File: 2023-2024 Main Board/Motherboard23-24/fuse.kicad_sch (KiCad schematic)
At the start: 20 parts, among them J22 Conn_01x02_Male

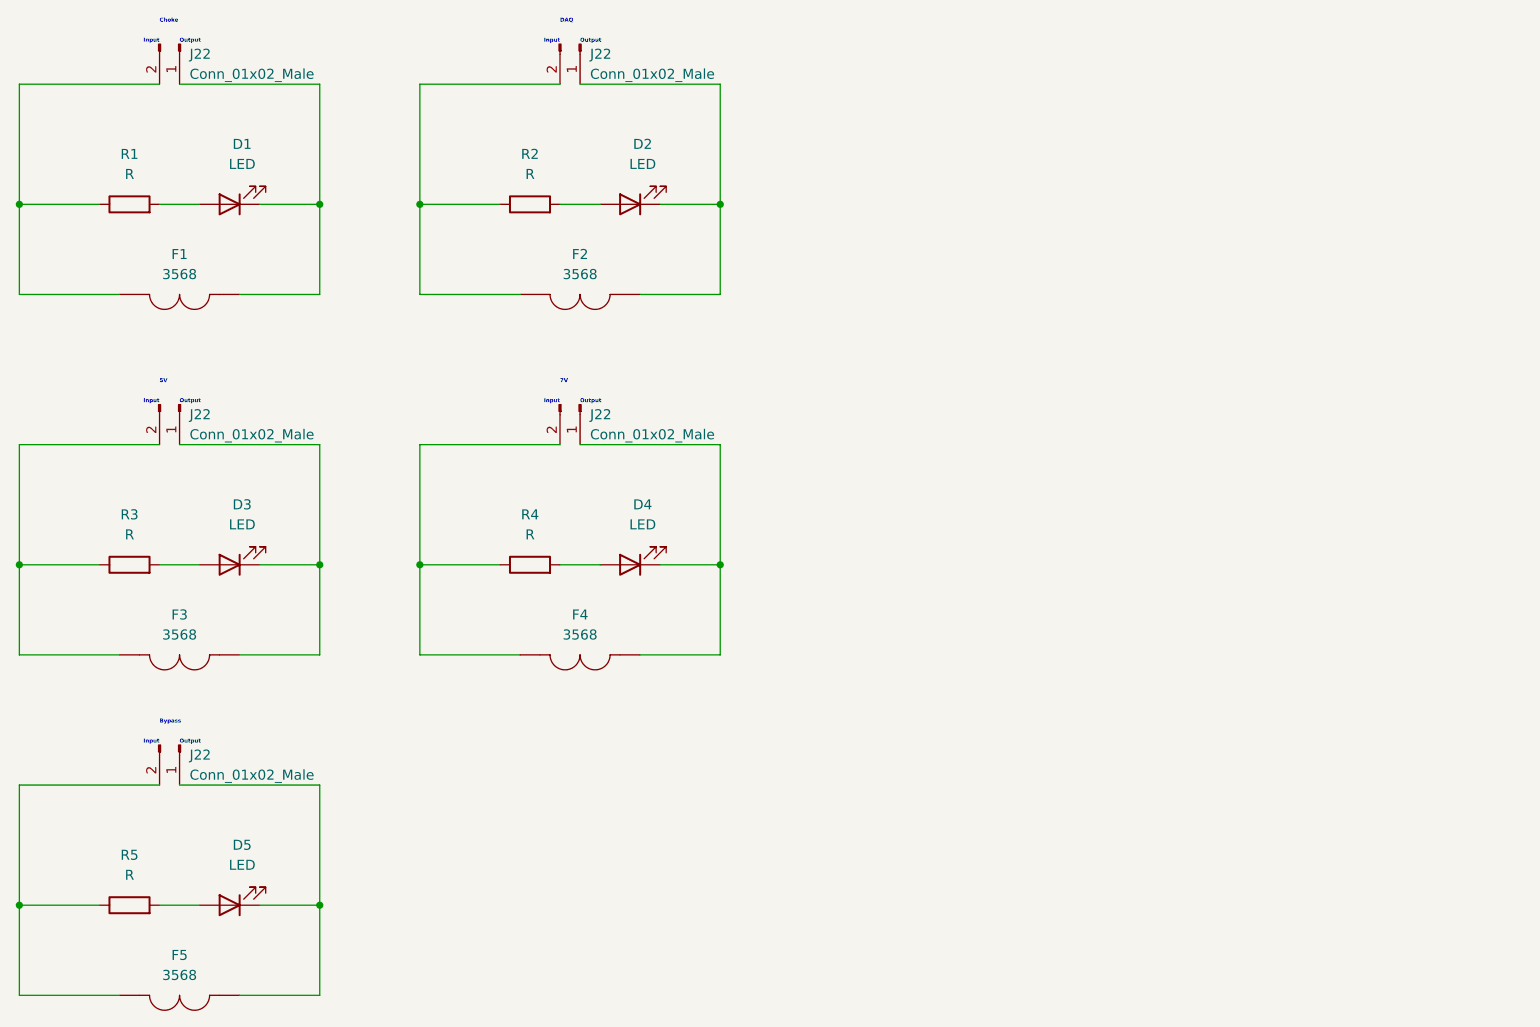
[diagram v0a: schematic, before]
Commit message: Added Schematic for Steering and Throttle
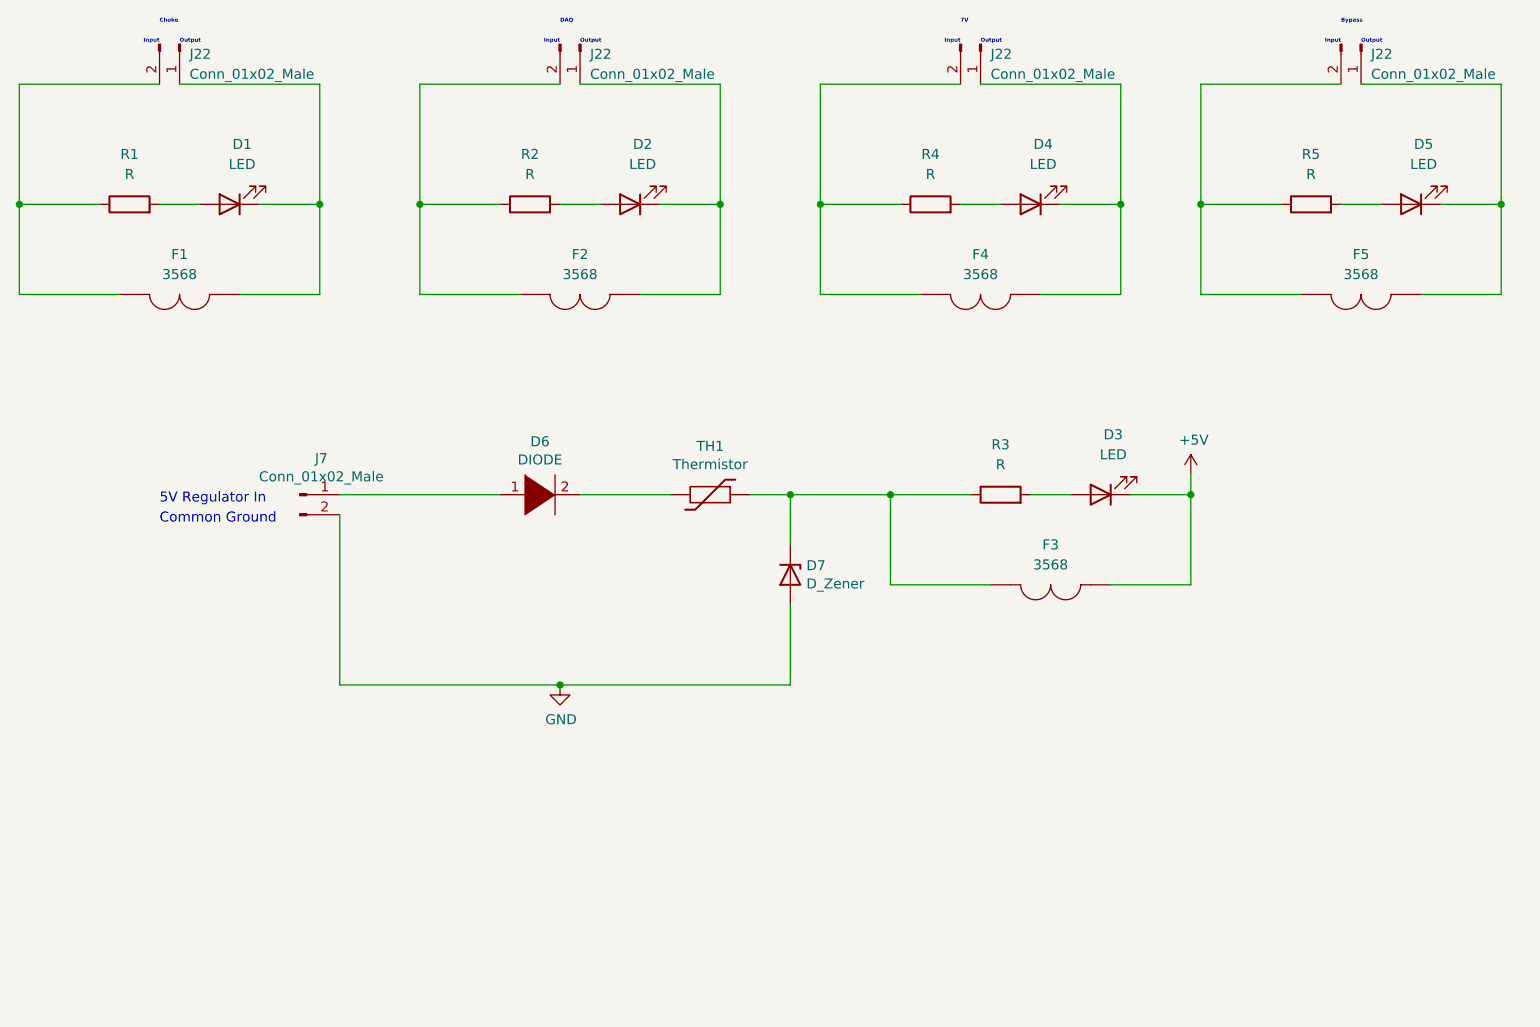
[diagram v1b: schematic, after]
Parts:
- removed J22: Conn_01x02_Male, TerminalBlock_Phoenix:TerminalBlock_Phoenix_MKDS-1,5-2-5.08_1x02_P5.08mm_Horizontal, symbol Motherboard_2023-rescue:Conn_01x02_Male-Connector
- added D6: DIODE, Diode_THT:D_DO-15_P5.08mm_Vertical_KathodeUp, symbol Motherboard_2023-rescue:DIODE-pspice
- added D7: D_Zener, Diode_THT:D_DO-15_P5.08mm_Vertical_KathodeUp, symbol Device:D_Zener
- added J7: Conn_01x02_Male, TerminalBlock_Phoenix:TerminalBlock_Phoenix_MKDS-1,5-2-5.08_1x02_P5.08mm_Horizontal, symbol Motherboard_2023-rescue:Conn_01x02_Male-Connector
- added TH1: Thermistor, Resistor_THT:R_Axial_DIN0414_L11.9mm_D4.5mm_P5.08mm_Vertical, symbol Device:Thermistor
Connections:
- net +5V: now reaches D3.1 (K), F3.2, F3.4
- net at F3.1, F3.3, R3.1: now also D7.1 (K), TH1.1
- new net: D6.1 (K), J7.1 (Pin_1)
- new net: D6.2 (A), TH1.2
- new net GND: D7.2 (A), J7.2 (Pin_2)
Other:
- note added: "5V Regulator In"
- note added: "Common Ground"
- note removed: "5V"
- moved on the sheet: D3, D4, D5, F3, F4, F5, J22, R3, R4, R5

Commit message: Close to finishing up 2023-2024 Main Board Schematic
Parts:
- renumbered D6 to D8, D7 to D9, J7 to J9, TH1 to TH2
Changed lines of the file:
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@@
   (symbol (lib_id "power:+5V") (at 194.31 107.95 0) (unit 1)
     (in_bom yes) (on_board yes) (dnp no)
-    (property "Reference" "#PWR02" (at 194.31 111.76 0)
+    (property "Reference" "#PWR04" (at 194.31 111.76 0)
       (effects (font (size 1.27 1.27)) hide)
     )
@@
   (symbol (lib_id "power:GND") (at 114.3 134.62 0) (unit 1)
     (in_bom yes) (on_board yes) (dnp no)
-    (property "Reference" "#PWR01" (at 114.3 140.97 0)
+    (property "Reference" "#PWR03" (at 114.3 140.97 0)
       (effects (font (size 1.27 1.27)) hide)
     )
@@
   (symbol (lib_id "Motherboard_2023-rescue:Conn_01x02_Male-Connector") (at 81.28 110.49 0) (unit 1)
     (in_bom yes) (on_board yes) (dnp no)
-    (property "Reference" "J7" (at 84.0232 105.8926 0)
+    (property "Reference" "J9" (at 84.0232 105.8926 0)
       (effects (font (size 1.27 1.27)))
     )
@@
   (symbol (lib_id "Device:Thermistor") (at 133.35 110.49 270) (unit 1)
     (in_bom yes) (on_board yes) (dnp no)
-    (property "Reference" "TH1" (at 133.35 104.3432 90)
+    (property "Reference" "TH2" (at 133.35 104.3432 90)
       (effects (font (size 1.27 1.27)))
     )
@@
   (symbol (lib_id "Device:D_Zener") (at 143.51 120.65 270) (unit 1)
     (in_bom yes) (on_board yes) (dnp no)
-    (property "Reference" "D7" (at 145.542 119.4816 90)
+    (property "Reference" "D9" (at 145.542 119.4816 90)
       (effects (font (size 1.27 1.27)) (justify left))
     )
@@
   (symbol (lib_id "Motherboard_2023-rescue:DIODE-pspice") (at 111.76 110.49 0) (unit 1)
     (in_bom yes) (on_board yes) (dnp no)
-    (property "Reference" "D6" (at 111.76 103.759 0)
-      (effects (font (size 1.27 1.27)))
-    )
+    (property "Reference" "D8" (at 111.76 103.759 0)
+      (effects (font (size 1.27 1.27)))
+    )

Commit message: first draft of 23-24 Main Board
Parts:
- D1, D2, D3, D4, D5: footprint (none) -> LED_THT:LED_D5.0mm
- F1, F2, F3, F4, F5: footprint FUSE_3568 -> 3568 (Fuse Holder):FUSE_3568
- R1, R2, R3, R4, R5: value R -> 1k; footprint (none) -> Resistor_THT:R_Axial_DIN0207_L6.3mm_D2.5mm_P10.16mm_Horizontal
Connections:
- net +5V: now also D5.1 (K); no longer D3.1 (K)
- net at R3.2: now also D5.2 (A); no longer D3.2 (A)
- net at R5.2: now also D4.2 (A); no longer D5.2 (A)
- net at F4.2, F4.4, J22.1 (Pin_1): now also D3.1 (K); no longer D4.1 (K)
- net at F5.2, F5.4, J22.1 (Pin_1): now also D4.1 (K); no longer D5.1 (K)
- net at R4.2: now also D3.2 (A); no longer D4.2 (A)
